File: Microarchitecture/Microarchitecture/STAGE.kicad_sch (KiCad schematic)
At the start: 4 parts

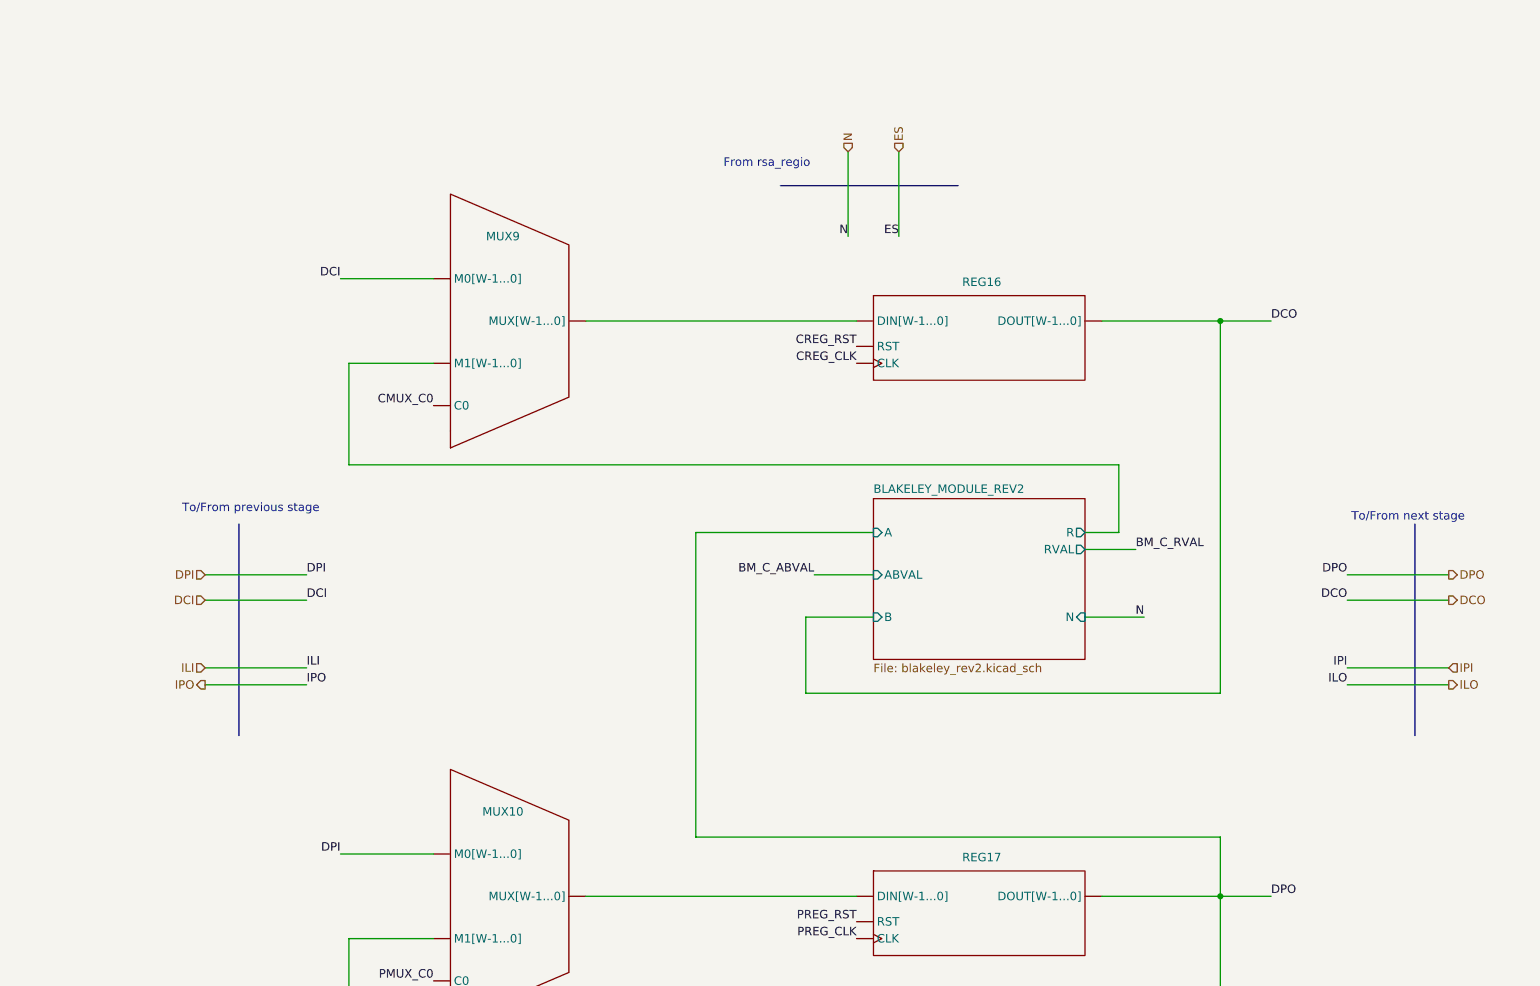
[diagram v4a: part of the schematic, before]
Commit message: Added comments, 16 to 8 stage pipeline
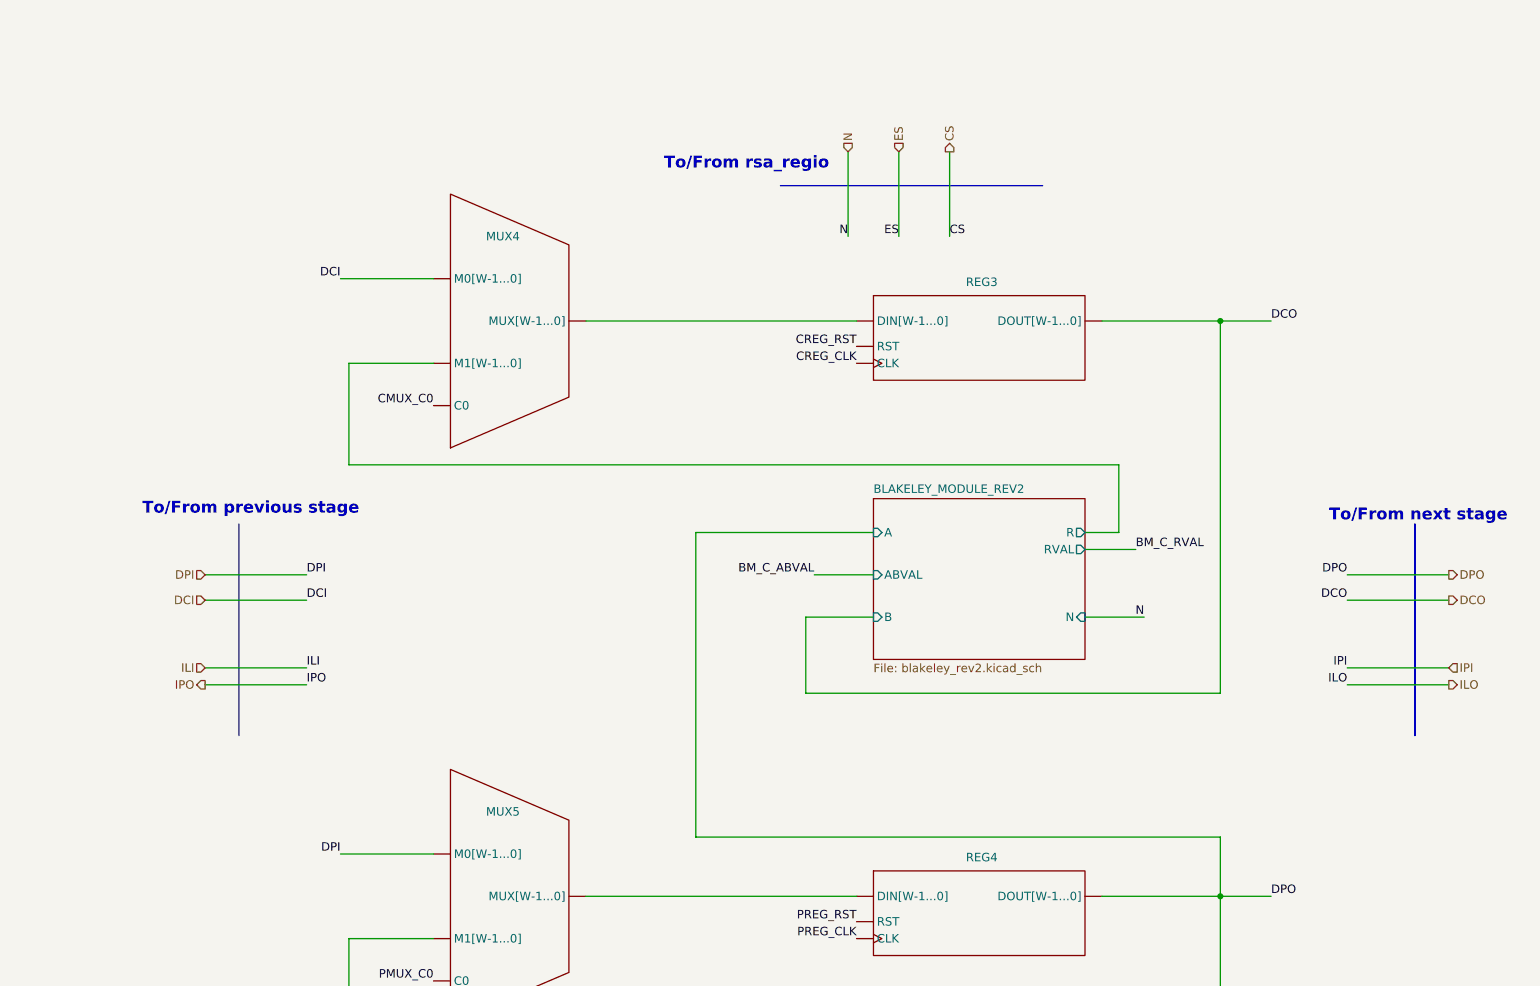
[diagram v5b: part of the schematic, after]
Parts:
- renumbered MUX9 to MUX4, MUX10 to MUX5, REG16 to REG3, REG17 to REG4
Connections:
- new net: MUX5. (MUX[W-1...0]), REG4. (RST)
- new net: MUX4. (MUX[W-1...0]), REG3. (RST)
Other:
- note added: "To/From rsa_regio"
- note removed: "From rsa_regio"
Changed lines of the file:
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@@
 	(wire
 		(pts
+			(xy 314.96 38.1) (xy 314.96 50.8)
+		)
+		(stroke
+			(width 0.508)
+			(type default)
+		)
+	)
+	(wire
+		(pts
 			(xy 374.65 105.41) (xy 389.89 105.41)
 		)
@@
 	(polyline
 		(pts
-			(xy 289.56 43.18) (xy 316.23 43.18)
+			(xy 289.56 43.18) (xy 328.93 43.18)
 		)
 		(stroke
@@
 		)
 	)
+	(polyline
+		(pts
+			(xy 384.81 93.98) (xy 384.81 125.73)
+		)
+		(stroke
+			(width 0)
+			(type default)
+		)
+	)
 	(wire
 		(pts
@@
 	(image
 		(at 143.51 241.3)
-		(scale 0.58991)
+		(scale 0.352348)
 		(data "iVBORw0KGgoAAAANSUhEUgAACVEAAAK8CAYAAADsh23GAAAAAXNSR0IArs4c6QAAAARnQU1BAACx"
 			"jwv8YQUAAAAJcEhZcwAAFiUAABYlAUlSJPAAAP+lSURBVHhe7P0PbFT3ne//v20mLNT1jrG/tKak"
@@
 		)
 	)
-	(text "Interfacing with blakeley_module:\n1: ABVAL 0->1\n2: WAIT FOR RVAL = 1\n3: ABVAL 1->0\n4: RVAL will then go low\nTHe sequence is interruptable with RST."
+	(text "To/From next stage"
 		(exclude_from_sim no)
-		(at 144.272 165.608 0)
+		(at 385.318 92.71 0)
 		(effects
 			(font
-				(size 1.27 1.27)
+				(size 1.778 1.778)
+				(thickness 0.3556)
+				(bold yes)
 			)
 		)
 	)
-	(text "Old rev 1 BLAKELEY_MODULE ->"
+	(text "Interfacing with blakeley_module:\n1: ABVAL 0->1\n2: WAIT FOR RVAL = 1\n3: ABVAL 1->0\n4: RVAL will then go low\nTHe sequence is interruptable with RST."
 		(exclude_from_sim no)
-		(at 39.624 28.194 0)
+		(at 144.272 165.608 0)
 		(effects
 			(font
@@
 		)
 	)
-	(text "From rsa_regio"
+	(text "Old rev 1 BLAKELEY_MODULE ->"
 		(exclude_from_sim no)
-		(at 287.528 39.878 0)
+		(at 39.624 28.194 0)
 		(effects
 			(font
@@
 		)
 	)
-	(text "To/From previous stage"
+	(text "To/From rsa_regio"
 		(exclude_from_sim no)
-		(at 210.058 91.694 0)
+		(at 284.48 39.878 0)
 		(effects
 			(font
-				(size 1.27 1.27)
+				(size 1.778 1.778)
+				(thickness 0.3556)
+				(bold yes)
 			)
 		)
 	)
-	(text "To/From next stage"
+	(text "To/From previous stage"
 		(exclude_from_sim no)
-		(at 383.794 92.964 0)
+		(at 210.058 91.694 0)
 		(effects
 			(font
-				(size 1.27 1.27)
+				(size 1.778 1.778)
+				(thickness 0.3556)
+				(bold yes)
 			)
 		)
@@
 		)
 	)
+	(label "CS"
+		(at 314.96 50.8 0)
+		(fields_autoplaced yes)
+		(effects
+			(font
+				(size 1.27 1.27)
+			)
+			(justify left bottom)
+		)
+	)
 	(label "CREG_CLK"
 		(at 300.99 69.85 180)
@@
 		)
 	)
+	(hierarchical_label "CS"
+		(shape output)
+		(at 314.96 38.1 90)
+		(fields_autoplaced yes)
+		(effects
+			(font
+				(size 1.27 1.27)
+			)
+			(justify left)
+		)
+	)
 	(hierarchical_label "DPO"
 		(shape output)
@@
 		(on_board yes)
 		(dnp no)
-		(property "Reference" "MUX10"
+		(property "Reference" "MUX5"
 			(at 247.904 137.16 0)
 			(effects
@@
 		(instances
 			(project "Microarchitecture"
-				(path "/7e18b03f-0dd8-4430-9873-65919f4f0c9c/21c2d8ae-34c8-4eeb-a025-0344b2d7e18d/2ff9fb5f-e895-4ed8-9926-01fc2395a11b"
-					(reference "MUX10")
-					(unit 1)
-				)
 				(path "/7e18b03f-0dd8-4430-9873-65919f4f0c9c/21c2d8ae-34c8-4eeb-a025-0344b2d7e18d/5c7540d9-7028-48a5-955b-0e835a2154cd"
 					(reference "MUX5")
 					(unit 1)
 				)
+				(path "/7e18b03f-0dd8-4430-9873-65919f4f0c9c/21c2d8ae-34c8-4eeb-a025-0344b2d7e18d/e302ed0c-39da-421e-9623-874dea47c4a1"
+					(reference "MUX9")
+					(unit 1)
+				)
+				(path "/7e18b03f-0dd8-4430-9873-65919f4f0c9c/21c2d8ae-34c8-4eeb-a025-0344b2d7e18d/e99a11b0-1092-4064-b05e-d34c79915b42"
+					(reference "MUX27")
+					(unit 1)
+				)
 			)
 		)
@@
 		(on_board yes)
 		(dnp no)
-		(property "Reference" "REG16"
+		(property "Reference" "REG3"
 			(at 319.786 57.658 0)
 			(effects
@@
 		(instances
 			(project "Microarchitecture"
-				(path "/7e18b03f-0dd8-4430-9873-65919f4f0c9c/21c2d8ae-34c8-4eeb-a025-0344b2d7e18d/2ff9fb5f-e895-4ed8-9926-01fc2395a11b"
-					(reference "REG16")
-					(unit 1)
-				)
 				(path "/7e18b03f-0dd8-4430-9873-65919f4f0c9c/21c2d8ae-34c8-4eeb-a025-0344b2d7e18d/5c7540d9-7028-48a5-955b-0e835a2154cd"
-					(reference "REG4")
+					(reference "REG3")
 					(unit 1)
 				)
@@
 					(unit 1)
 				)
+				(path "/7e18b03f-0dd8-4430-9873-65919f4f0c9c/21c2d8ae-34c8-4eeb-a025-0344b2d7e18d/e302ed0c-39da-421e-9623-874dea47c4a1"
+					(reference "REG5")
+					(unit 1)
+				)
+				(path "/7e18b03f-0dd8-4430-9873-65919f4f0c9c/21c2d8ae-34c8-4eeb-a025-0344b2d7e18d/e99a11b0-1092-4064-b05e-d34c79915b42"
+					(reference "REG40")
+					(unit 1)
+				)
 			)
 		)
@@
 		(on_board yes)
 		(dnp no)
-		(property "Reference" "REG17"
+		(property "Reference" "REG4"
 			(at 319.786 144.018 0)
 			(effects
@@
 		(instances
 			(project "Microarchitecture"
-				(path "/7e18b03f-0dd8-4430-9873-65919f4f0c9c/21c2d8ae-34c8-4eeb-a025-0344b2d7e18d/2ff9fb5f-e895-4ed8-9926-01fc2395a11b"
-					(reference "REG17")
-					(unit 1)
-				)
 				(path "/7e18b03f-0dd8-4430-9873-65919f4f0c9c/21c2d8ae-34c8-4eeb-a025-0344b2d7e18d/5c7540d9-7028-48a5-955b-0e835a2154cd"
-					(reference "REG6")
+					(reference "REG4")
 					(unit 1)
 				)
@@
 					(unit 1)
 				)
+				(path "/7e18b03f-0dd8-4430-9873-65919f4f0c9c/21c2d8ae-34c8-4eeb-a025-0344b2d7e18d/e302ed0c-39da-421e-9623-874dea47c4a1"
+					(reference "REG6")
+					(unit 1)
+				)
+				(path "/7e18b03f-0dd8-4430-9873-65919f4f0c9c/21c2d8ae-34c8-4eeb-a025-0344b2d7e18d/e99a11b0-1092-4064-b05e-d34c79915b42"
+					(reference "REG41")
+					(unit 1)
+				)
 			)
 		)
@@
 		(on_board yes)
 		(dnp no)
-		(property "Reference" "MUX9"
+		(property "Reference" "MUX4"
 			(at 247.904 50.8 0)
 			(effects
@@
 		(instances
 			(project "Microarchitecture"
-				(path "/7e18b03f-0dd8-4430-9873-65919f4f0c9c/21c2d8ae-34c8-4eeb-a025-0344b2d7e18d/2ff9fb5f-e895-4ed8-9926-01fc2395a11b"
-					(reference "MUX9")
-					(unit 1)
-				)
 				(path "/7e18b03f-0dd8-4430-9873-65919f4f0c9c/21c2d8ae-34c8-4eeb-a025-0344b2d7e18d/5c7540d9-7028-48a5-955b-0e835a2154cd"
 					(reference "MUX4")
@@
 					(unit 1)
 				)
+				(path "/7e18b03f-0dd8-4430-9873-65919f4f0c9c/21c2d8ae-34c8-4eeb-a025-0344b2d7e18d/e302ed0c-39da-421e-9623-874dea47c4a1"
+					(reference "MUX7")
+					(unit 1)
+				)
+				(path "/7e18b03f-0dd8-4430-9873-65919f4f0c9c/21c2d8ae-34c8-4eeb-a025-0344b2d7e18d/e99a11b0-1092-4064-b05e-d34c79915b42"
+					(reference "MUX26")
+					(unit 1)
+				)
 			)
 		)
@@
 					(page "10")
 				)
-				(path "/7e18b03f-0dd8-4430-9873-65919f4f0c9c/21c2d8ae-34c8-4eeb-a025-0344b2d7e18d/2ff9fb5f-e895-4ed8-9926-01fc2395a11b"
-					(page "13")
+				(path "/7e18b03f-0dd8-4430-9873-65919f4f0c9c/21c2d8ae-34c8-4eeb-a025-0344b2d7e18d/e99a11b0-1092-4064-b05e-d34c79915b42"
+					(page "35")
+				)
+				(path "/7e18b03f-0dd8-4430-9873-65919f4f0c9c/21c2d8ae-34c8-4eeb-a025-0344b2d7e18d/e302ed0c-39da-421e-9623-874dea47c4a1"
+					(page "16")
 				)
 			)
@@
 					(page "15")
 				)
+				(path "/7e18b03f-0dd8-4430-9873-65919f4f0c9c/21c2d8ae-34c8-4eeb-a025-0344b2d7e18d/e99a11b0-1092-4064-b05e-d34c79915b42"
+					(page "34")
+				)
+				(path "/7e18b03f-0dd8-4430-9873-65919f4f0c9c/21c2d8ae-34c8-4eeb-a025-0344b2d7e18d/e302ed0c-39da-421e-9623-874dea47c4a1"
+					(page "14")
+				)
 			)
 		)
@@
 					(page "11")
 				)
-				(path "/7e18b03f-0dd8-4430-9873-65919f4f0c9c/21c2d8ae-34c8-4eeb-a025-0344b2d7e18d/2ff9fb5f-e895-4ed8-9926-01fc2395a11b"
-					(page "14")
+				(path "/7e18b03f-0dd8-4430-9873-65919f4f0c9c/21c2d8ae-34c8-4eeb-a025-0344b2d7e18d/e99a11b0-1092-4064-b05e-d34c79915b42"
+					(page "33")
+				)
+				(path "/7e18b03f-0dd8-4430-9873-65919f4f0c9c/21c2d8ae-34c8-4eeb-a025-0344b2d7e18d/e302ed0c-39da-421e-9623-874dea47c4a1"
+					(page "13")
 				)
 			)

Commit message: Tried to update tb
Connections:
- new net: MUX5. (MUX[W-1...0]), REG4. (RST)
- new net: MUX4. (MUX[W-1...0]), REG3. (RST)
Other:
- sheet BLAKELEY_MODULE_REV2 ports: added NX1, NX2; removed N
- sheet BLAKELEY_MODULE_REV3 ports: added NX1, NX2; removed N
- note added: "To/From rsa_core"
- note removed: "To/From rsa_regio"
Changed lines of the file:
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@@
 	(wire
 		(pts
-			(xy 307.34 38.1) (xy 307.34 50.8)
+			(xy 304.8 36.83) (xy 304.8 49.53)
 		)
 		(stroke
@@
 	(wire
 		(pts
+			(xy 320.04 36.83) (xy 320.04 49.53)
+		)
+		(stroke
+			(width 0.508)
+			(type default)
+		)
+	)
+	(wire
+		(pts
 			(xy 335.28 95.25) (xy 340.36 95.25)
 		)
@@
 	(wire
 		(pts
+			(xy 335.28 106.68) (xy 342.9 106.68)
+		)
+		(stroke
+			(width 0.508)
+			(type default)
+		)
+	)
+	(wire
+		(pts
 			(xy 355.6 149.86) (xy 355.6 140.97)
 		)
@@
 	(wire
 		(pts
-			(xy 224.79 85.09) (xy 224.79 69.85)
+			(xy 312.42 36.83) (xy 312.42 49.53)
 		)
 		(stroke
@@
 	(wire
 		(pts
-			(xy 276.86 95.25) (xy 303.53 95.25)
+			(xy 224.79 85.09) (xy 224.79 69.85)
 		)
 		(stroke
@@
 	(wire
 		(pts
-			(xy 280.67 194.31) (xy 280.67 181.61)
+			(xy 276.86 95.25) (xy 303.53 95.25)
 		)
 		(stroke
@@
 	(wire
 		(pts
-			(xy 374.65 118.11) (xy 389.89 118.11)
+			(xy 280.67 194.31) (xy 280.67 181.61)
 		)
 		(stroke
-			(width 0)
+			(width 0.508)
 			(type default)
 		)
@@
 	(wire
 		(pts
-			(xy 223.52 57.15) (xy 237.49 57.15)
+			(xy 374.65 118.11) (xy 389.89 118.11)
 		)
 		(stroke
-			(width 0.508)
+			(width 0)
 			(type default)
 		)
@@
 	(wire
 		(pts
-			(xy 314.96 38.1) (xy 314.96 50.8)
+			(xy 223.52 57.15) (xy 237.49 57.15)
 		)
 		(stroke
@@
 		)
 	)
-	(wire
+	(polyline
 		(pts
-			(xy 299.72 38.1) (xy 299.72 50.8)
+			(xy 299.72 41.91) (xy 332.74 41.91)
 		)
 		(stroke
-			(width 0.508)
+			(width 0)
 			(type default)
 		)
 	)
-	(polyline
+	(wire
 		(pts
-			(xy 289.56 43.18) (xy 328.93 43.18)
+			(xy 335.28 193.04) (xy 342.9 193.04)
 		)
 		(stroke
-			(width 0)
+			(width 0.508)
 			(type default)
 		)
@@
 	(wire
 		(pts
-			(xy 335.28 107.95) (xy 344.17 107.95)
+			(xy 374.65 101.6) (xy 389.89 101.6)
 		)
 		(stroke
@@
 	(wire
 		(pts
-			(xy 374.65 101.6) (xy 389.89 101.6)
+			(xy 335.28 196.85) (xy 342.9 196.85)
 		)
 		(stroke
@@
 	(wire
 		(pts
-			(xy 335.28 194.31) (xy 342.9 194.31)
+			(xy 355.6 140.97) (xy 276.86 140.97)
 		)
 		(stroke
@@
 	(wire
 		(pts
-			(xy 355.6 140.97) (xy 276.86 140.97)
+			(xy 335.28 181.61) (xy 340.36 181.61)
 		)
 		(stroke
@@
 	(wire
 		(pts
-			(xy 335.28 181.61) (xy 340.36 181.61)
+			(xy 218.44 101.6) (xy 203.2 101.6)
 		)
 		(stroke
@@
 	(wire
 		(pts
-			(xy 218.44 101.6) (xy 203.2 101.6)
+			(xy 335.28 110.49) (xy 342.9 110.49)
 		)
 		(stroke
@@
 	(wire
 		(pts
+			(xy 327.66 36.83) (xy 327.66 49.53)
+		)
+		(stroke
+			(width 0.508)
+			(type default)
+		)
+	)
+	(wire
+		(pts
 			(xy 337.82 63.5) (xy 355.6 63.5)
 		)
@@
 	)
 	(image
-		(at 143.51 241.3)
+		(at 90.17 251.46)
 		(scale 0.352348)
 		(data "iVBORw0KGgoAAAANSUhEUgAACVEAAAK8CAYAAADsh23GAAAAAXNSR0IArs4c6QAAAARnQU1BAACx"
@@
 		)
 	)
-	(text "To/From rsa_regio"
+	(text "To/From rsa_core"
 		(exclude_from_sim no)
-		(at 284.48 39.878 0)
+		(at 290.576 39.116 0)
 		(effects
 			(font
@@
 	)
 	(label "ES"
-		(at 307.34 50.8 180)
+		(at 304.8 49.53 0)
 		(fields_autoplaced yes)
 		(effects
@@
 				(size 1.27 1.27)
 			)
-			(justify right bottom)
+			(justify left bottom)
 		)
 	)
-	(label "CS"
-		(at 314.96 50.8 0)
+	(label "NX2"
+		(at 342.9 110.49 0)
 		(fields_autoplaced yes)
 		(effects
@@
 		)
 	)
-	(label "N"
-		(at 342.9 194.31 180)
-		(fields_autoplaced yes)
-		(effects
-			(font
-				(size 1.27 1.27)
-			)
-			(justify right bottom)
-		)
-	)
 	(label "DCI"
 		(at 223.52 57.15 180)
@@
 		)
 	)
+	(label "NX1"
+		(at 342.9 106.68 0)
+		(fields_autoplaced yes)
+		(effects
+			(font
+				(size 1.27 1.27)
+			)
+			(justify left bottom)
+		)
+	)
 	(label "CMUX_C0"
 		(at 237.49 76.2 180)
@@
 		)
 	)
-	(label "N"
-		(at 344.17 107.95 180)
+	(label "DCO"
+		(at 363.22 63.5 0)
 		(fields_autoplaced yes)
 		(effects
@@
 				(size 1.27 1.27)
 			)
-			(justify right bottom)
+			(justify left bottom)
 		)
 	)
-	(label "N"
-		(at 299.72 50.8 180)
+	(label "RSM_STATUS"
+		(at 327.66 49.53 0)
 		(fields_autoplaced yes)
 		(effects
@@
 				(size 1.27 1.27)
 			)
-			(justify right bottom)
+			(justify left bottom)
 		)
 	)
-	(label "DCO"
-		(at 363.22 63.5 0)
+	(label "NX1"
+		(at 342.9 193.04 0)
+		(fields_autoplaced yes)
+		(effects
+			(font
+				(size 1.27 1.27)
+			)
+			(justify left bottom)
+		)
+	)
+	(label "NX1"
+		(at 312.42 49.53 0)
+		(fields_autoplaced yes)
+		(effects
+			(font
+				(size 1.27 1.27)
+			)
+			(justify left bottom)
+		)
+	)
+	(label "NX2"
+		(at 342.9 196.85 0)
 		(fields_autoplaced yes)
 		(effects
@@
 		)
 	)
+	(label "NX2"
+		(at 320.04 49.53 0)
+		(fields_autoplaced yes)
+		(effects
+			(font
+				(size 1.27 1.27)
+			)
+			(justify left bottom)
+		)
+	)
 	(label "PREG_CLK"
 		(at 300.99 156.21 180)
@@
 		)
 	)
-	(hierarchical_label "ILO"
-		(shape output)
-		(at 389.89 118.11 0)
+	(hierarchical_label "STATUS"
+		(shape input)
+		(at 327.66 36.83 90)
 		(fields_autoplaced yes)
 		(effects
@@
 		)
 	)
-	(hierarchical_label "IPO"
+	(hierarchical_label "ILO"
 		(shape output)
-		(at 203.2 118.11 180)
+		(at 389.89 118.11 0)
 		(fields_autoplaced yes)
 		(effects
@@
 				(size 1.27 1.27)
 			)
-			(justify right)
+			(justify left)
 		)
 	)
-	(hierarchical_label "N"
-		(shape input)
-		(at 299.72 38.1 90)
+	(hierarchical_label "IPO"
+		(shape output)
+		(at 203.2 118.11 180)
 		(fields_autoplaced yes)
 		(effects
@@
 				(size 1.27 1.27)
 			)
-			(justify left)
+			(justify right)
 		)
 	)
@@
 		)
 	)
+	(hierarchical_label "NX1"
+		(shape input)
+		(at 312.42 36.83 90)
+		(fields_autoplaced yes)
+		(effects
+			(font
+				(size 1.27 1.27)
+			)
+			(justify left)
+		)
+	)
 	(hierarchical_label "ILI"
 		(shape input)
@@
 	(hierarchical_label "ES"
 		(shape input)
-		(at 307.34 38.1 90)
+		(at 304.8 36.83 90)
 		(fields_autoplaced yes)
 		(effects
@@
 		)
 	)
-	(hierarchical_label "CS"
-		(shape output)
-		(at 314.96 38.1 90)
+	(hierarchical_label "NX2"
+		(shape input)
+		(at 320.04 36.83 90)
 		(fields_autoplaced yes)
 		(effects
@@
 			)
 		)
-		(pin "N" input
-			(at 335.28 107.95 0)
+		(pin "R" output
+			(at 335.28 95.25 0)
 			(effects
 				(font
@@
 			)
 		)
-		(pin "R" output
-			(at 335.28 95.25 0)
+		(pin "RVAL" output
+			(at 335.28 97.79 0)
 			(effects
 				(font
@@
 			)
 		)
-		(pin "RVAL" output
-			(at 335.28 97.79 0)
+		(pin "NX1" input
+			(at 335.28 106.68 0)
+			(effects
+				(font
+					(size 1.27 1.27)
+				)
+				(justify right)
+			)
+		)
+		(pin "NX2" input
+			(at 335.28 110.49 0)
 			(effects
 				(font
@@
 			)
 		)
-		(pin "N" input
-			(at 335.28 194.31 0)
+		(pin "R" output
+			(at 335.28 181.61 0)
 			(effects
 				(font
@@
 			)
 		)
-		(pin "R" output
-			(at 335.28 181.61 0)
+		(pin "RVAL" output
+			(at 335.28 184.15 0)
 			(effects
 				(font
@@
 			)
 		)
-		(pin "RVAL" output
-			(at 335.28 184.15 0)
+		(pin "NX1" input
+			(at 335.28 193.04 0)
+			(effects
+				(font
+					(size 1.27 1.27)
+				)
+				(justify right)
+			)
+		)
+		(pin "NX2" input
+			(at 335.28 196.85 0)
 			(effects
 				(font
